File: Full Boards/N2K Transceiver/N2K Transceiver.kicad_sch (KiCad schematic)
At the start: 74 parts, among them J3 JTAG, SW1 SW_MEC_5G, SW2 SW_MEC_5G, SW3 SW_MEC_5G

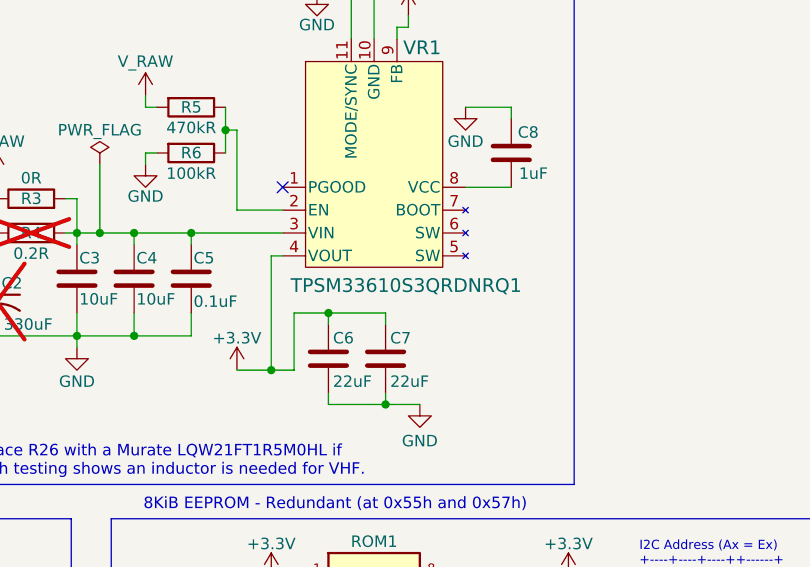
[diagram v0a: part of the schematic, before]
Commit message: Swapped 1A VR for 600mA version.
Signed-off-by: digimer <digital.mermaid@gmail.com>
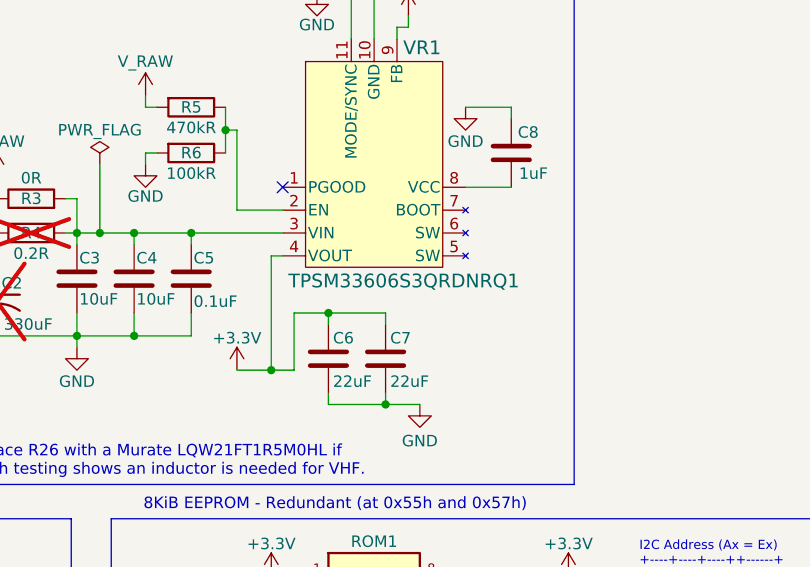
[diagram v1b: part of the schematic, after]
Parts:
- VR1: value TPSM33610S3QRDNRQ1 -> TPSM33606S3QRDNRQ1
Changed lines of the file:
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@@
 			)
 		)
-		(property "Value" "TPSM33610S3QRDNRQ1"
-			(at 209.296 52.832 0)
+		(property "Value" "TPSM33606S3QRDNRQ1"
+			(at 209.042 52.324 0)
 			(show_name no)
 			(do_not_autoplace no)

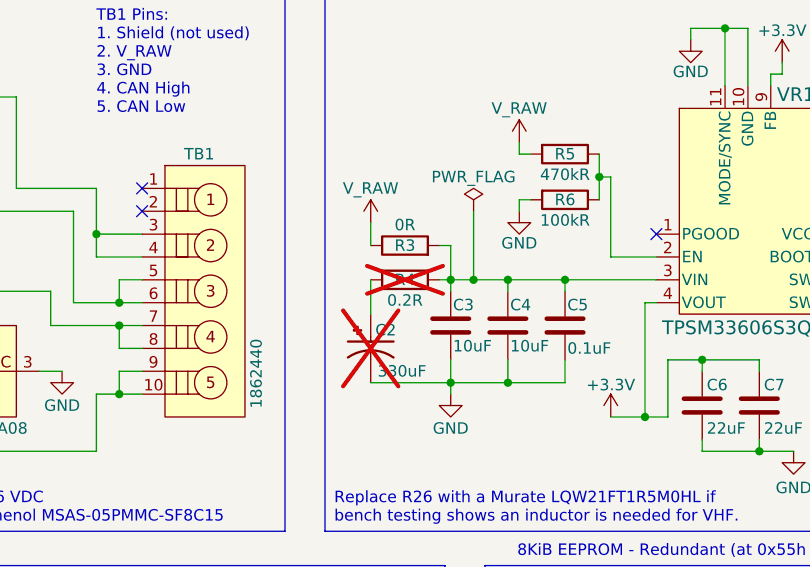
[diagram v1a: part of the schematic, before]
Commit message: Fixed old symbol for the Panasonic EEH-ZU1V331V cap.
Signed-off-by: digimer <digital.mermaid@gmail.com>
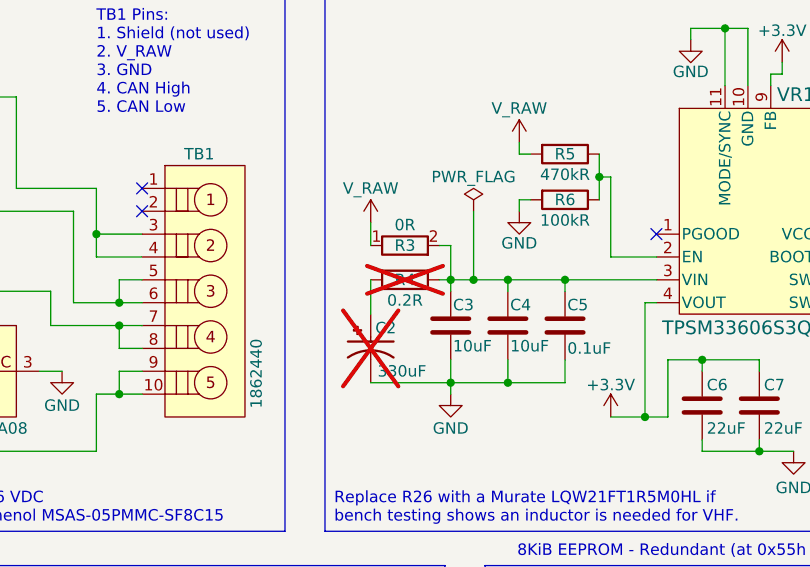
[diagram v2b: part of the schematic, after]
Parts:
- C2: symbol mr-parts:Panasonic EEH-ZU -> mr-parts:Panasonic EEH-ZU1V331V; MANUFACTURER Panasonic -> (none); MAXIMUM_PACKAGE_HEIGHT 12.8mm -> (none); PARTREV 30-Sep-20 -> (none); Part (none) -> Panasonic EEH-ZU1V331V; STANDARD Manufacturer Recommendations -> (none); now in the parts list
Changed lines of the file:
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@@
 	)
 	(symbol
-		(lib_id "mr-parts:Panasonic EEH-ZU")
+		(lib_id "mr-parts:Panasonic EEH-ZU1V331V")
 		(at 163.83 53.34 270)
 		(unit 1)
 		(body_style 1)
 		(exclude_from_sim no)
-		(in_bom no)
+		(in_bom yes)
 		(on_board yes)
 		(in_pos_files yes)
 		(dnp yes)
 		(property "Reference" "C2"
-			(at 164.338 52.578 90)
+			(at 164.338 53.086 90)
 			(show_name no)
 			(do_not_autoplace no)
@@
 					(size 1.27 1.27)
 				)
-				(justify left)
+				(justify left bottom)
 			)
 		)
@@
 			)
 		)
-		(property "PARTREV" "30-Sep-20"
-			(at 152.146 53.34 0)
-			(hide yes)
-			(show_name no)
-			(do_not_autoplace no)
-			(effects
-				(font
-					(size 1.27 1.27)
-				)
-				(justify bottom)
-			)
-		)
-		(property "STANDARD" "Manufacturer Recommendations"
-			(at 156.718 53.34 0)
-			(hide yes)
-			(show_name no)
-			(do_not_autoplace no)
-			(effects
-				(font
-					(size 1.27 1.27)
-				)
-				(justify bottom)
-			)
-		)
-		(property "MAXIMUM_PACKAGE_HEIGHT" "12.8mm"
-			(at 147.828 53.34 0)
-			(hide yes)
-			(show_name no)
-			(do_not_autoplace no)
-			(effects
-				(font
-					(size 1.27 1.27)
-				)
-				(justify bottom)
-			)
-		)
-		(property "MANUFACTURER" "Panasonic"
+		(property "Part" "Panasonic EEH-ZU1V331V"
 			(at 150.114 53.34 0)
 			(hide yes)

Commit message: Cleaned up silkscreen.
Signed-off-by: digimer <digital.mermaid@gmail.com>
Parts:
- renumbered J3 to J1, TP3 to TP2
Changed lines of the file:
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@@
 	(title_block
 		(title "N2K Transceiver")
-		(date "2026-09-07")
+		(date "2026-09-11")
 		(rev "1.0.0")
 		(company "The Digital Mermaid")
@@
 		(in_pos_files yes)
 		(dnp yes)
-		(property "Reference" "TP3"
+		(property "Reference" "TP2"
 			(at 26.416 20.32 90)
 			(show_name no)
@@
 			(project "N2K Transceiver"
 				(path "/2a070473-cb6e-4844-8f2a-5ea6a35ddb49"
-					(reference "TP3")
+					(reference "TP2")
 					(unit 1)
 				)
@@
 		(in_pos_files yes)
 		(dnp yes)
-		(property "Reference" "J3"
+		(property "Reference" "J1"
 			(at 96.52 122.174 90)
 			(show_name no)
@@
 			(project "N2K Transceiver"
 				(path "/2a070473-cb6e-4844-8f2a-5ea6a35ddb49"
-					(reference "J3")
+					(reference "J1")
 					(unit 1)
 				)

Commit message: Removed the DNP'ed RC damper. With the TVS, it should not be possible for ringing to raise the voltage above 40v.
Signed-off-by: digimer <digital.mermaid@gmail.com>
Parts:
- removed C2: 330uF, mr-stuff:Panasonic EEH-ZU, symbol mr-parts:Panasonic EEH-ZU1V331V
- removed R4: 0.2R, mr-stuff:KOA SR73, symbol mr-parts:KOA Speer SR732BTTDR200F
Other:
- moved on the sheet: R3

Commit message: Updated annotations after the RC removal.
Signed-off-by: digimer <digital.mermaid@gmail.com>
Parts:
- renumbered C11 to C10, C12 to C11, C13 to C12, C14 to C13, C15 to C14, C3 to C2, C4 to C3, C5 to C4, C6 to C5, C7 to C6, C8 to C7, C9 to C8, C10 to C9, R11 to R10, R12 to R11, R13 to R12, R14 to R13, R15 to R14, R16 to R15, R17 to R16, R18 to R17, R19 to R18, R20 to R19, R21 to R20, R22 to R21, R23 to R22, R24 to R23, R25 to R24, R26 to R25, R27 to R26, R5 to R4, R6 to R5, R7 to R6, R8 to R7, R9 to R8, R10 to R9
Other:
- note added: "Replace R3 with a Murate LQW21FT1R5M0HL if bench testing shows an inductor is needed for VHF."
- note removed: "Replace R26 with a Murate LQW21FT1R5M0HL if bench testing shows an inductor is needed for VHF."

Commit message: Made the VR1 mode selectable via 0 ohm resistors.
Signed-off-by: digimer <digital.mermaid@gmail.com>
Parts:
- added R3, R4: 0R, mr-stuff:Vishay RCA-SR e3, symbol mr-parts:Vishay RCA08050000ZSEASR
- renumbered R8 to R10, R9 to R11, R10 to R12, R11 to R13, R12 to R14, R13 to R15, R14 to R16, R15 to R17, R16 to R18, R17 to R19, R18 to R20, R19 to R21, R20 to R22, R21 to R23, R22 to R24, R23 to R25, R24 to R26, R25 to R27, R26 to R28, R4 to R5, R5 to R6, R3 to R7, R6 to R8, R7 to R9
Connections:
- net GND: now also R4.2; no longer VR1.11 (MODE/SYNC)
- net V_RAW: now also R3.1
- new net: R3.2, R4.1, VR1.11 (MODE/SYNC)
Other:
- note added: "Populate R3 _or_ R4, not both! R3: Forces PWM mode; consistent 2.2MHz switching. Noisier, but consistently so. VHF squelch may be quieter. R4: Auto mode; switches to PFM (bursts, 50 KHz) under 10~15% load (60~90mA). Expected that this board will live in that boundary, possibly resulting in frequent PWM <-> FPWM transitions. Bench testing required. Decide and hard wire for final production."

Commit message: Added 100pF cap near VR1 to help with VHF noise suppression.
Signed-off-by: digimer <digital.mermaid@gmail.com>
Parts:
- added C5: 100pF, mr-stuff:Kemet C0805X, symbol mr-parts:Kemet C0805X101J5GACAUTO
- renumbered C9 to C10, C10 to C11, C11 to C12, C12 to C13, C13 to C14, C14 to C15, C5 to C6, C6 to C7, C7 to C8, C8 to C9
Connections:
- net GND: now also C5.2
- net V_RAW: now also R7.2; no longer R7.1
- net at C2.1, C3.1, C4.1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: now also R7.1, C5.1; no longer R7.2
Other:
- moved on the sheet: C2, C3, C4, R7

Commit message: Added a second 100pF cap to the VR1's output +3.3V rail.
Signed-off-by: digimer <digital.mermaid@gmail.com>
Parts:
- added C6: 100pF, mr-stuff:Kemet C0805X, symbol mr-parts:Kemet C0805X101J5GACAUTO
- renumbered C9 to C10, C10 to C11, C11 to C12, C12 to C13, C13 to C14, C14 to C16, C15 to C17, C6 to C7, C7 to C8, C8 to C9
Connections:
- net +3.3V: now also C6.1
- net GND: now also C6.2
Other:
- moved on the sheet: C7, C8
